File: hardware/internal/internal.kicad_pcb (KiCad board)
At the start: 2 copper layers, 40 x 38.3 mm, 25 parts, among them T1 TestPoint_THTPad_3.0x3.0mm_Dr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, T12 TestPoint_THTPad_3.0x3.0mm_Dr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, T13 TestPoint_THTPad_3.0x3.0mm_Dr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, T14 TestPoint_THTPad_3.0x3.0mm_Dr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, T15 TestPoint_THTPad_3.0x3.0mm_Dr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, T16 TestPoint_THTPad_3.0x3.0mm_Dr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, T18 TestPoint_THTPad_3.0x3.0mm_Dr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, T19 TestPoint_THTPad_3.0x3.0mm_Dr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, T20 TestPoint_THTPad_3.0x3.0mm_Dr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, T21 TestPoint_THTPad_3.0x3.0mm_Dr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, T22 TestPoint_THTPad_3.0x3.0mm_Dr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, T51 TestPoint_THTPad_D2.0mm_Drill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, T52 TestPoint_THTPad_D2.0mm_Drill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, T53 TestPoint_THTPad_D2.0mm_Drill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, T54 TestPoint_THTPad_D2.0mm_Drill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, T55 TestPoint_THTPad_D2.0mm_Drill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, T56 TestPoint_THTPad_D2.0mm_Drill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

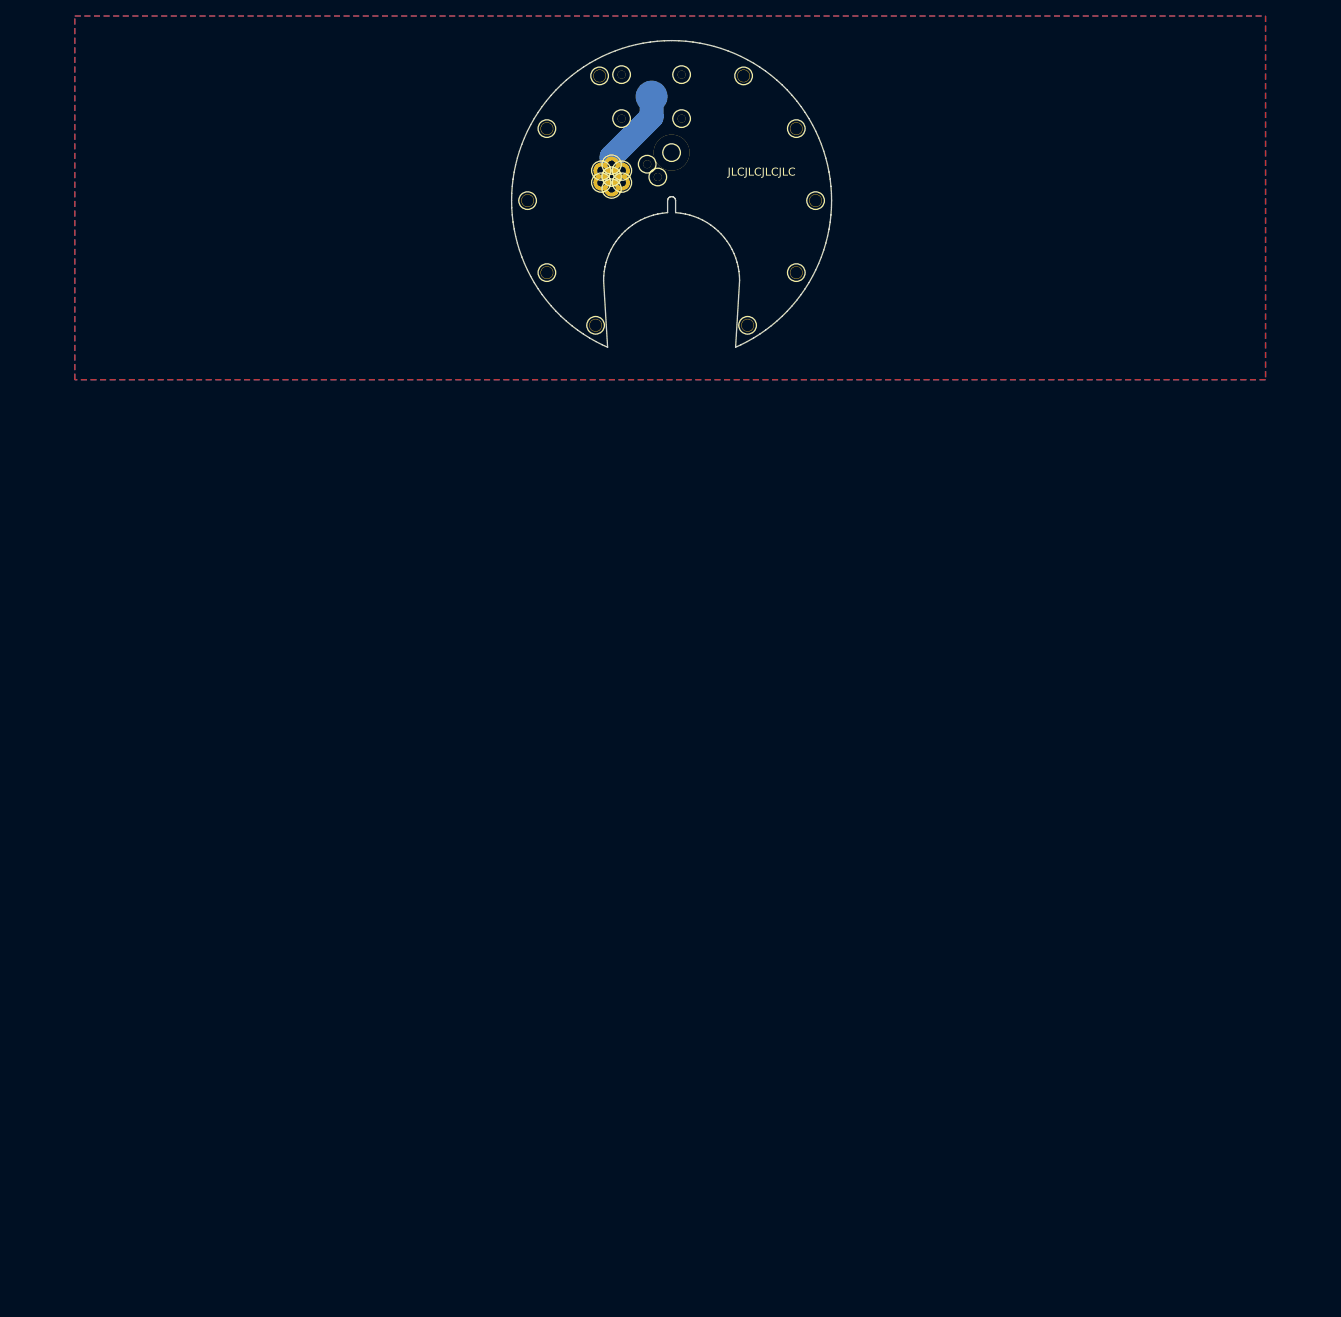
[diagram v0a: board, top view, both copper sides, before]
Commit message: separate boards and generate fab files
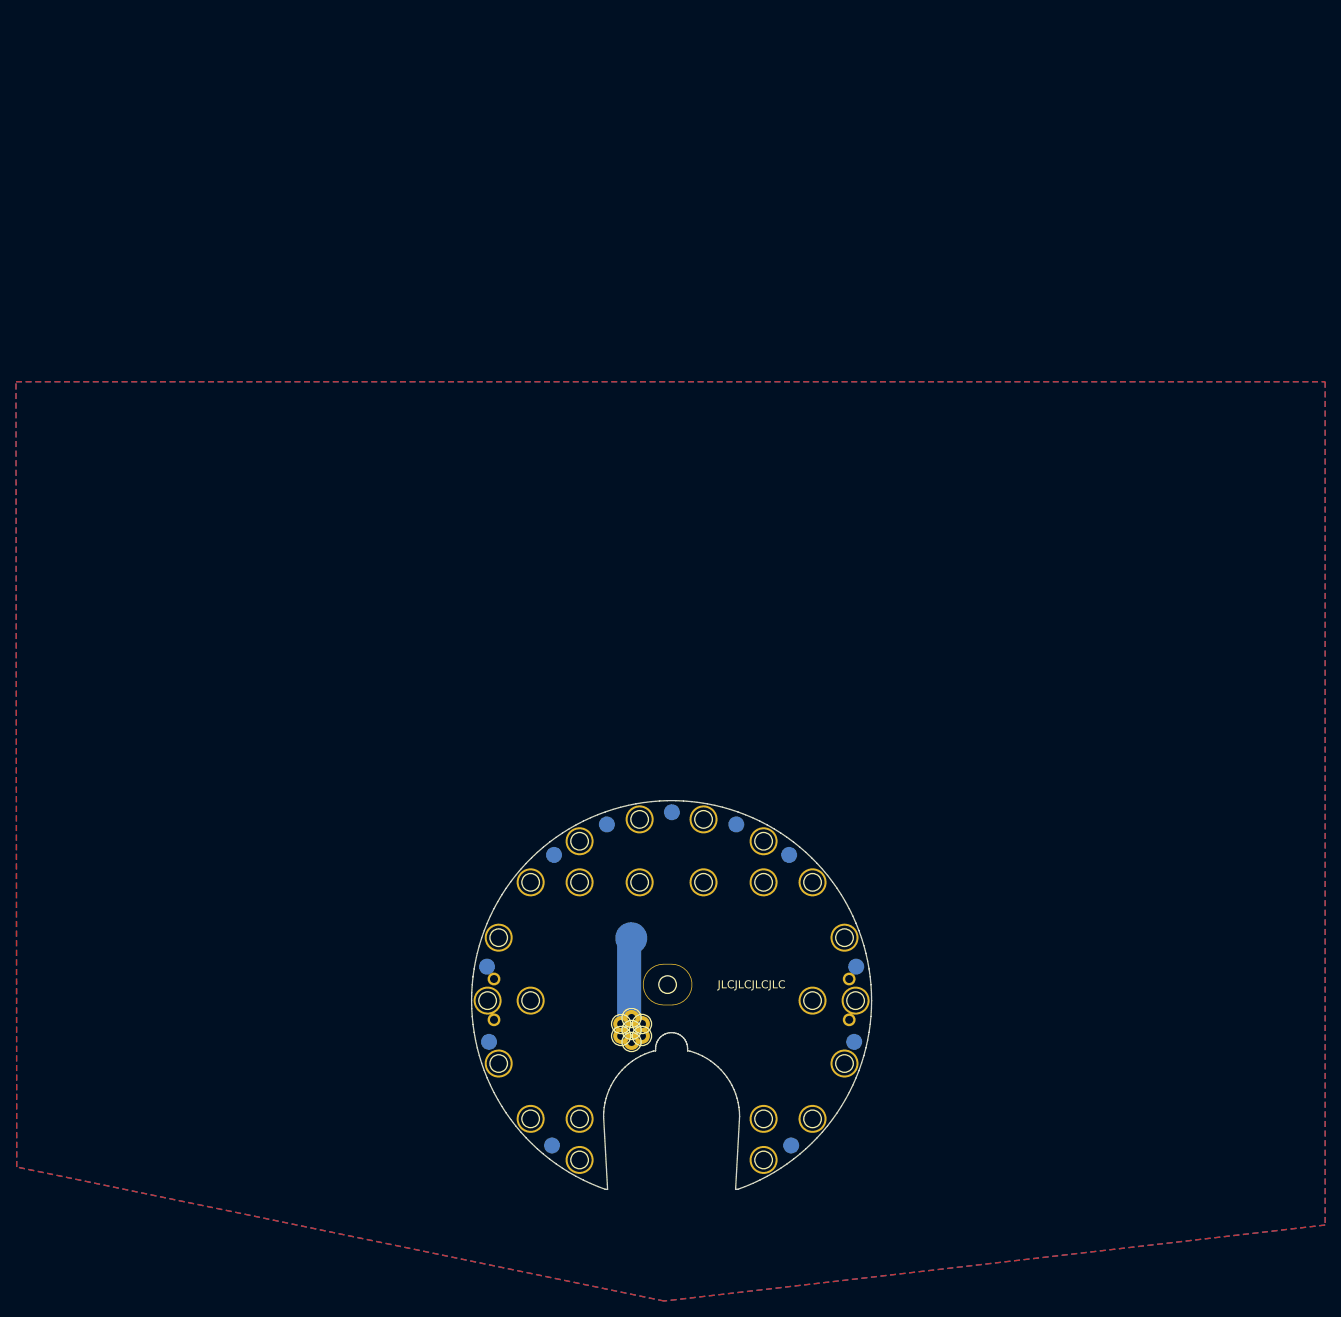
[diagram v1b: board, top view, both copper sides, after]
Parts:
- removed T12, T13, T14, T15, T16, T18, T19, T20, T21 (x7), T22: TestPoint_THTPad_3.0x3.0mm_Drill1.5mm, TestPoint:TestPoint_THTPad_3.0x3.0mm_Drill1.5mm
- added align-io1: , , F.Cu at (77.8, 147.3)
- added align-io2: , , F.Cu at (122.2, 152.4)
- added align-ir1: , , F.Cu at (77.8, 152.4)
- added align-ir2: , , F.Cu at (122.2, 147.3)
- added clearance-D1: TestPoint_THTPad_3.0x3.0mm_Drill1.5mm, TestPoint:TestPoint_THTPad_3.0x3.0mm_Drill1.5mm, F.Cu at (88.5, 169.9)
- added clearance-D10: TestPoint_THTPad_3.0x3.0mm_Drill1.5mm, TestPoint:TestPoint_THTPad_3.0x3.0mm_Drill1.5mm, F.Cu at (111.5, 130.1)
- added clearance-D11: TestPoint_THTPad_3.0x3.0mm_Drill1.5mm, TestPoint:TestPoint_THTPad_3.0x3.0mm_Drill1.5mm, F.Cu at (117.6, 135.2)
- added clearance-D12: TestPoint_THTPad_3.0x3.0mm_Drill1.5mm, TestPoint:TestPoint_THTPad_3.0x3.0mm_Drill1.5mm, F.Cu at (121.6, 142.1)
- added clearance-D13: TestPoint_THTPad_3.0x3.0mm_Drill1.5mm, TestPoint:TestPoint_THTPad_3.0x3.0mm_Drill1.5mm, F.Cu at (123.0, 150.0)
- added clearance-D14: TestPoint_THTPad_3.0x3.0mm_Drill1.5mm, TestPoint:TestPoint_THTPad_3.0x3.0mm_Drill1.5mm, F.Cu at (121.6, 157.9)
- added clearance-D15: TestPoint_THTPad_3.0x3.0mm_Drill1.5mm, TestPoint:TestPoint_THTPad_3.0x3.0mm_Drill1.5mm, F.Cu at (117.6, 164.8)
- added clearance-D16: TestPoint_THTPad_3.0x3.0mm_Drill1.5mm, TestPoint:TestPoint_THTPad_3.0x3.0mm_Drill1.5mm, F.Cu at (111.5, 169.9)
- added clearance-D2: TestPoint_THTPad_3.0x3.0mm_Drill1.5mm, TestPoint:TestPoint_THTPad_3.0x3.0mm_Drill1.5mm, F.Cu at (82.4, 164.8)
- added clearance-D3: TestPoint_THTPad_3.0x3.0mm_Drill1.5mm, TestPoint:TestPoint_THTPad_3.0x3.0mm_Drill1.5mm, F.Cu at (78.4, 157.9)
- added clearance-D4: TestPoint_THTPad_3.0x3.0mm_Drill1.5mm, TestPoint:TestPoint_THTPad_3.0x3.0mm_Drill1.5mm, F.Cu at (77.0, 150.0)
- added clearance-D5: TestPoint_THTPad_3.0x3.0mm_Drill1.5mm, TestPoint:TestPoint_THTPad_3.0x3.0mm_Drill1.5mm, F.Cu at (78.4, 142.1)
- added clearance-D6: TestPoint_THTPad_3.0x3.0mm_Drill1.5mm, TestPoint:TestPoint_THTPad_3.0x3.0mm_Drill1.5mm, F.Cu at (82.4, 135.2)
- added clearance-D7: TestPoint_THTPad_3.0x3.0mm_Drill1.5mm, TestPoint:TestPoint_THTPad_3.0x3.0mm_Drill1.5mm, F.Cu at (88.5, 130.1)
- added clearance-D8: TestPoint_THTPad_3.0x3.0mm_Drill1.5mm, TestPoint:TestPoint_THTPad_3.0x3.0mm_Drill1.5mm, F.Cu at (96.0, 127.3)
- added clearance-D9: TestPoint_THTPad_3.0x3.0mm_Drill1.5mm, TestPoint:TestPoint_THTPad_3.0x3.0mm_Drill1.5mm, F.Cu at (104.0, 127.3)
- added clearance-R1: TestPoint_THTPad_3.0x3.0mm_Drill1.5mm, TestPoint:TestPoint_THTPad_3.0x3.0mm_Drill1.5mm, F.Cu at (88.5, 164.8)
- added clearance-R2: TestPoint_THTPad_3.0x3.0mm_Drill1.5mm, TestPoint:TestPoint_THTPad_3.0x3.0mm_Drill1.5mm, F.Cu at (82.4, 150.0)
- added clearance-R3: TestPoint_THTPad_3.0x3.0mm_Drill1.5mm, TestPoint:TestPoint_THTPad_3.0x3.0mm_Drill1.5mm, F.Cu at (88.5, 135.2)
- added clearance-R4: TestPoint_THTPad_3.0x3.0mm_Drill1.5mm, TestPoint:TestPoint_THTPad_3.0x3.0mm_Drill1.5mm, F.Cu at (96.0, 135.2)
- added clearance-R5: TestPoint_THTPad_3.0x3.0mm_Drill1.5mm, TestPoint:TestPoint_THTPad_3.0x3.0mm_Drill1.5mm, F.Cu at (104.0, 135.2)
- added clearance-R6: TestPoint_THTPad_3.0x3.0mm_Drill1.5mm, TestPoint:TestPoint_THTPad_3.0x3.0mm_Drill1.5mm, F.Cu at (111.5, 135.2)
- added clearance-R7: TestPoint_THTPad_3.0x3.0mm_Drill1.5mm, TestPoint:TestPoint_THTPad_3.0x3.0mm_Drill1.5mm, F.Cu at (117.6, 150.0)
- added clearance-R8: TestPoint_THTPad_3.0x3.0mm_Drill1.5mm, TestPoint:TestPoint_THTPad_3.0x3.0mm_Drill1.5mm, F.Cu at (111.5, 164.8)
- added stitch2: TestPoint_Pad_D2.0mm, TestPoint:TestPoint_Pad_D2.0mm, B.Cu at (114.9, 168.1)
- added stitch2: TestPoint_Pad_D2.0mm, TestPoint:TestPoint_Pad_D2.0mm, B.Cu at (77.2, 155.2)
- added stitch2: TestPoint_Pad_D2.0mm, TestPoint:TestPoint_Pad_D2.0mm, B.Cu at (85.1, 168.1)
- added stitch2: TestPoint_Pad_D2.0mm, TestPoint:TestPoint_Pad_D2.0mm, B.Cu at (100.0, 126.5)
- added stitch2: TestPoint_Pad_D2.0mm, TestPoint:TestPoint_Pad_D2.0mm, B.Cu at (122.8, 155.2)
- added stitch2: TestPoint_Pad_D2.0mm, TestPoint:TestPoint_Pad_D2.0mm, B.Cu at (85.3, 131.8)
- added stitch2: TestPoint_Pad_D2.0mm, TestPoint:TestPoint_Pad_D2.0mm, B.Cu at (114.7, 131.8)
- added stitch2: TestPoint_Pad_D2.0mm, TestPoint:TestPoint_Pad_D2.0mm, B.Cu at (91.9, 128.0)
- added stitch2: TestPoint_Pad_D2.0mm, TestPoint:TestPoint_Pad_D2.0mm, B.Cu at (123.1, 145.8)
- added stitch2: TestPoint_Pad_D2.0mm, TestPoint:TestPoint_Pad_D2.0mm, B.Cu at (76.9, 145.8)
- added stitch2: TestPoint_Pad_D2.0mm, TestPoint:TestPoint_Pad_D2.0mm, B.Cu at (108.1, 128.0)
- moved through-i1 106.7 mm to (95.0, 153.7)
- moved through-i2 106.7 mm to (95.0, 152.2)
- moved through-i3 106.7 mm to (96.3, 152.9)
- moved through-i4 106.7 mm to (96.3, 154.4)
- moved through-i5 106.7 mm to (95.0, 155.2)
- moved through-i6 106.7 mm to (93.7, 154.4)
- moved through-i7 106.7 mm to (93.7, 152.9)
- moved contact-i1 105.2 mm to (95.0, 142.2)
- moved clearance-U1 104.0 mm to (99.5, 148.0)
- renumbered T1 to clearance-U1, REF** to contact-i1, T51 to through-i1, T51 to through-i2, T52 to through-i3, T53 to through-i4, T54 to through-i5, T55 to through-i6, T56 to through-i7
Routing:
- net +3V0: track 12.1 -> 13.2 mm
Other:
- board size 40 x 38.3 mm -> 50 x 48.6 mm
- board text added: "import QR SVG scale 0.2"

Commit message: separate into fab-able parts
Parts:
- moved align-io1 50.0 mm to (77.8, 97.3)
- moved align-ir2 50.0 mm to (122.2, 97.3)
- moved clearance-D1 50.0 mm to (88.5, 119.9)
- moved clearance-D11 50.0 mm to (117.6, 85.2)
- moved clearance-D14 50.0 mm to (121.6, 107.9)
- moved clearance-D16 50.0 mm to (111.5, 119.9)
- moved clearance-D3 50.0 mm to (78.4, 107.9)
- moved clearance-D6 50.0 mm to (82.4, 85.2)
- moved clearance-R1 50.0 mm to (88.5, 114.8)
- moved clearance-R8 50.0 mm to (111.5, 114.8)
- moved stitch2 50.0 mm to (114.9, 118.1)
- moved stitch2 50.0 mm to (85.1, 118.1)
- moved stitch2 50.0 mm to (85.3, 81.8)
- moved stitch2 50.0 mm to (114.7, 81.8)
- moved stitch2 50.0 mm to (123.1, 95.8)
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
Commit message: cleanup fab files
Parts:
- moved clearance-R2 7.00 mm to (82.4, 107.0)
- moved clearance-R7 7.00 mm to (117.6, 107.0)
- renumbered align-io1 to align-i1, align-ir2 to align-i2, align-ir1 to align-i3, align-io2 to align-i4
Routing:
- net +3V0: track 13.2 -> 14.2 mm
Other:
- board text removed: "import QR SVG scale 0.2"
